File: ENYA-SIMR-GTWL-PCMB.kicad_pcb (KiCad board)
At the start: 4 copper layers, 116.2 x 60 mm, 127 parts, among them J1 USB_A_RA, J10 PICO_BLADE_1x6_MALE_RA_SMD, J11 PICO_BLADE_1x6_MALE_RA_SMD, J12 PICO_BLADE_1x14_MALE_RA_SMD, J13 PICO_BLADE_1x14_MALE_RA_SMD, J14 USB_WIRE_POINT, J2 TC2050-FP_PROG, J3 PICO_BLADE_1x3_MALE_RA_SMD, J4 PICO_BLADE_1x3_MALE_RA_SMD, J5 PICO_BLADE_1x3_MALE_RA_SMD, J6 PICO_BLADE_1x3_MALE_RA_SMD, J7 PICO_BLADE_1x3_MALE_RA_SMD, J8 PICO_BLADE_1x5_MALE_RA_SMD, J9 PICO_BLADE_1x5_MALE_RA_SMD, Q9 2N7002, SW1 56DP30-01-1-AJN, SW2 56DP30-01-1-AJN, SW3 56DP30-01-1-AJN, SW4 56DP30-01-1-AJN, U1 USB2512B, U4 AP22653W6-7_ILIM_2.1A_SOT-23-6, U5 STM32F303RET6TR, U6 LM393BIDR, U7 MCP1725_3.3V_500mA_DFN-8, U8 TPD2EUSB30_5.5V_8V_SOT-3, U9 TPD2EUSB30_5.5V_8V_SOT-3, Y1 ABM10_24MHz_10pF_SMD4_2.5x2.0, Y2 ABM10_32MHz_10pF_SMD4_2.5x2.0

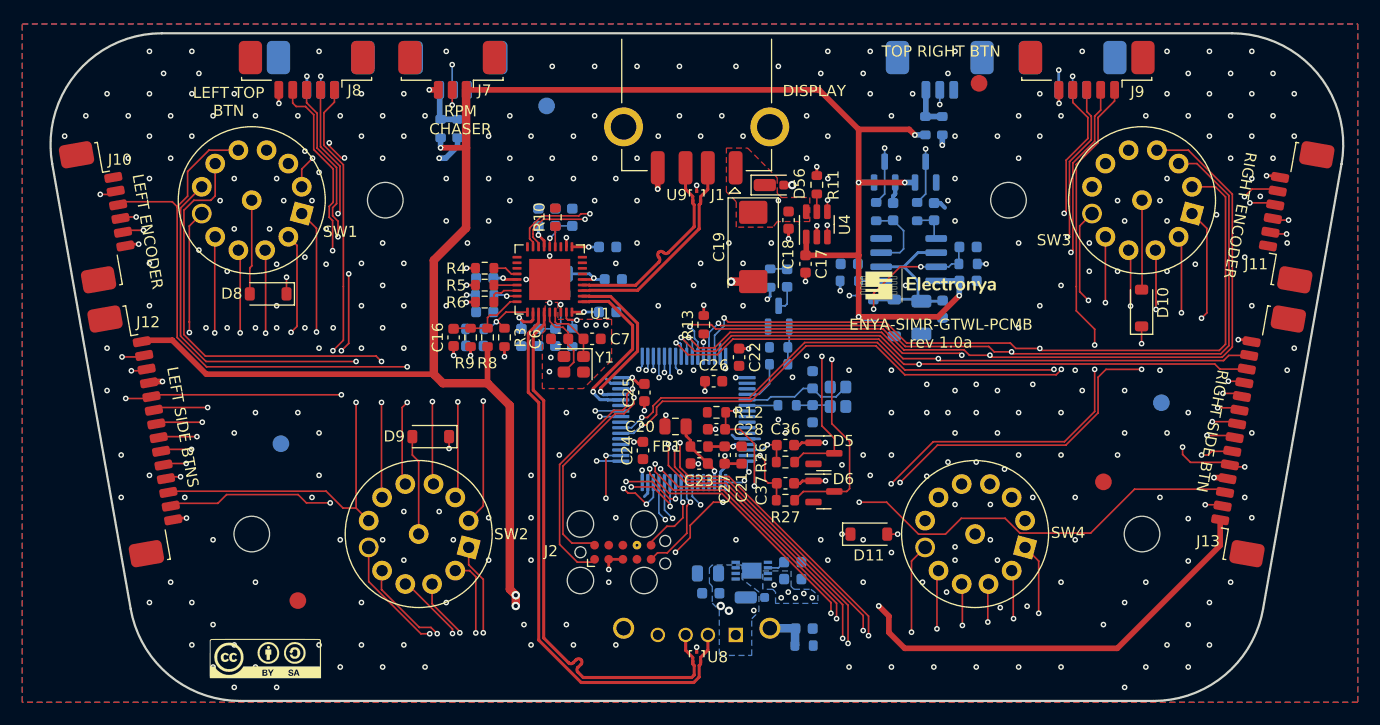
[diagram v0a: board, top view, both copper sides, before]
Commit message: rework for encoder instead of selector switch
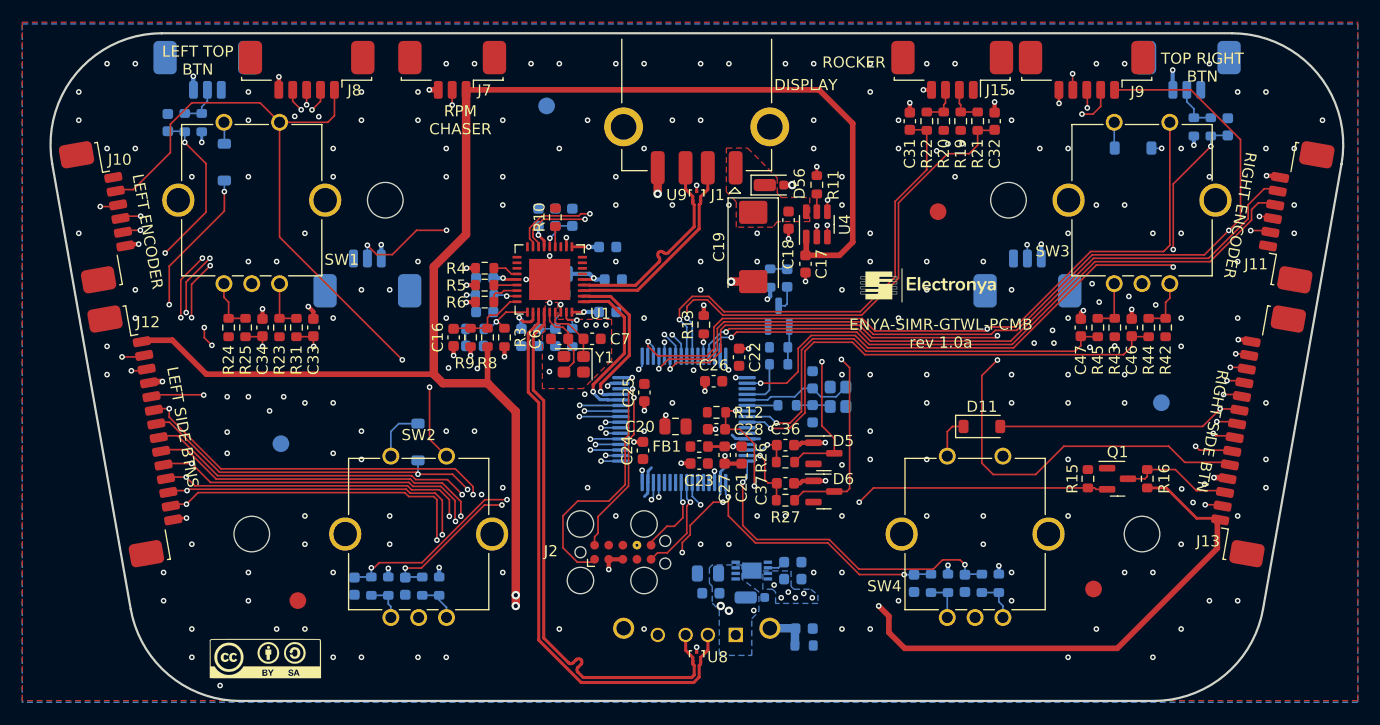
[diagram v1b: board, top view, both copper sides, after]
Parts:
- removed D3, D4: BAV99_SOT-23, Package_TO_SOT_SMD:SOT-23
- removed U6: LM393BIDR, Package_SO:SOIC-8_3.9x4.9mm_P1.27mm
- removed Z1: MMSZ5222BT1G, Diode_SMD:D_SOD-123
- added C45: 10nF_CER_0603_50V, Capacitor_SMD:C_0603_1608Metric, B.Cu at (177.8, 154.4)
- added C46: 10nF_CER_0603_50V, Capacitor_SMD:C_0603_1608Metric, F.Cu at (247.6, 131.2)
- added C47: 10nF_CER_0603_50V, Capacitor_SMD:C_0603_1608Metric, F.Cu at (243.1, 131.2)
- added C48: 10nF_CER_0603_50V, Capacitor_SMD:C_0603_1608Metric, B.Cu at (232.6, 154.2)
- added C49: 10nF_CER_0603_50V, Capacitor_SMD:C_0603_1608Metric, B.Cu at (228.1, 154.2)
- added J15: PICO_BLADE_1x4_MALE_RA_SMD, ENYA_Connector_PicoBlade:PICO_BLADE_53261_1x4_SMD_RA_1.25MM, F.Cu at (231.5, 106.9)
- added Q1: BSS138, Package_TO_SOT_SMD:SOT-23, F.Cu at (246.4, 144.8)
- added R19: 10K_0603_100MW, Resistor_SMD:R_0603_1608Metric, F.Cu at (232.3, 112.6)
- added R20: 10K_0603_100MW, Resistor_SMD:R_0603_1608Metric, F.Cu at (230.7, 112.6)
- added R21: 0R_0603_100MW, Resistor_SMD:R_0603_1608Metric, F.Cu at (233.8, 112.6)
- added R22: 0R_0603_100MW, Resistor_SMD:R_0603_1608Metric, F.Cu at (229.2, 112.6)
- added R23: 10K_0603_100MW, Resistor_SMD:R_0603_1608Metric, F.Cu at (171.0, 131.2)
- added R31: 10K_0603_100MW, Resistor_SMD:R_0603_1608Metric, F.Cu at (172.6, 131.2)
- added R32: 10K_0603_100MW, Resistor_SMD:R_0603_1608Metric, B.Cu at (185.4, 154.4)
- added R33: 10K_0603_100MW, Resistor_SMD:R_0603_1608Metric, B.Cu at (180.8, 154.4)
- added R34: 10K_0603_100MW, Resistor_SMD:R_0603_1608Metric, B.Cu at (183.9, 154.4)
- added R35: 10K_0603_100MW, Resistor_SMD:R_0603_1608Metric, B.Cu at (179.3, 154.4)
- added R36: 10K_0603_100MW, Resistor_SMD:R_0603_1608Metric, B.Cu at (235.7, 154.2)
- added R37: 10K_0603_100MW, Resistor_SMD:R_0603_1608Metric, B.Cu at (231.1, 154.2)
- added R38: 10K_0603_100MW, Resistor_SMD:R_0603_1608Metric, B.Cu at (234.2, 154.2)
- added R42: 10K_0603_100MW, Resistor_SMD:R_0603_1608Metric, F.Cu at (250.7, 131.2)
- added R43: 10K_0603_100MW, Resistor_SMD:R_0603_1608Metric, F.Cu at (246.1, 131.2)
- added R44: 10K_0603_100MW, Resistor_SMD:R_0603_1608Metric, F.Cu at (249.1, 131.2)
- added R45: 10K_0603_100MW, Resistor_SMD:R_0603_1608Metric, F.Cu at (244.6, 131.2)
- C31, C32, R24, R25: moved to F.Cu
- C33, C34: value 100nF_CER_0603_50V -> 10nF_CER_0603_50V; moved to F.Cu
- C35: value 10uF_CER_1206_25V -> 10nF_CER_0603_50V; footprint Capacitor_SMD:C_1206_3216Metric -> Capacitor_SMD:C_0603_1608Metric
- D10, D8, D9: moved to B.Cu
- R15, R16: value 0R_0603_100MW -> 10K_0603_100MW; moved to F.Cu
- R17, R18: value 0R_0603_100MW -> 10K_0603_100MW
- R39: value 124R_0603_100MW -> 10K_0603_100MW
- SW1, SW2, SW3, SW4: value 56DP30-01-1-AJN -> PEC11H-4015F-S0016; footprint ENYA_Switch_Selector:56DP30-01-1-AJN_1P_12T -> ENYA_Encoder:PEC11H_Switch_Vertical
- moved R16 69.5 mm to (249.0, 144.8)
- moved R15 66.1 mm to (243.7, 144.8), turned to -90 degrees
- moved C38 65.7 mm to (161.0, 112.8)
- moved R25 65.2 mm to (168.0, 131.2), turned to 90 degrees
- moved R17 65.0 mm to (164.1, 112.8)
- moved C34 63.8 mm to (169.5, 131.2), turned to 90 degrees
- moved R28 62.6 mm to (162.5, 112.8)
- moved R24 55.9 mm to (166.5, 131.2), turned to -90 degrees
- moved C35 52.3 mm to (182.3, 154.4)
- moved C33 48.5 mm to (174.1, 131.2), turned to 90 degrees
- moved C39 27.5 mm to (256.3, 113.2)
- moved R29 27.5 mm to (254.7, 113.2)
- moved R39 25.2 mm to (229.6, 154.2), turned to -90 degrees
- moved R18 22.6 mm to (253.2, 113.2)
- moved J6 22.2 mm to (252.6, 106.9)
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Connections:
- C31 pad 1: +2.5V -> /MCU/ROCKER_RIGHT
- C32 pad 1: +5V -> /MCU/ROCKER_LEFT
- C33 pad 1: /MCU/SHIFTER_DOWN -> /BUTTONS_ENCODERS_LEDS/TC_ENC_B
- C34 pad 1: /MCU/SHIFTER_UP -> /BUTTONS_ENCODERS_LEDS/TC_ENC_A
- C35 pad 1: +2.5V -> /BUTTONS_ENCODERS_LEDS/TC1_ENC_B
- C38 pad 1: Net-(U6A-+) -> /MCU/SHIFTER_DOWN
- C39 pad 1: Net-(U6B-+) -> /MCU/SHIFTER_UP
- D10 pad 1: /BUTTONS_ENCODERS_LEDS/BTN_COL2 -> Net-(D10-K)
- D10 pad 2: Net-(D10-A) -> /BUTTONS_ENCODERS_LEDS/BTN_ROW2
- D11 pad 1: /BUTTONS_ENCODERS_LEDS/BTN_COL3 -> Net-(D11-K)
- D11 pad 2: Net-(D11-A) -> /BUTTONS_ENCODERS_LEDS/BTN_ROW3
- D8 pad 1: /BUTTONS_ENCODERS_LEDS/BTN_COL0 -> Net-(D8-K)
- D8 pad 2: Net-(D8-A) -> /BUTTONS_ENCODERS_LEDS/BTN_ROW0
- D9 pad 1: /BUTTONS_ENCODERS_LEDS/BTN_COL1 -> Net-(D9-K)
- D9 pad 2: Net-(D9-A) -> /BUTTONS_ENCODERS_LEDS/BTN_ROW1
- J1 pad SH: Earth -> GND
- J10 pad 2: /BUTTONS_ENCODERS_LEDS/BTN_COL5 -> /BUTTONS_ENCODERS_LEDS/BTN_COL0
- J10 pad 3: /BUTTONS_ENCODERS_LEDS/BTN_ROW8 -> /BUTTONS_ENCODERS_LEDS/BTN_ROW7
- J11 pad 2: /BUTTONS_ENCODERS_LEDS/BTN_COL6 -> /BUTTONS_ENCODERS_LEDS/BTN_COL1
- J11 pad 3: /BUTTONS_ENCODERS_LEDS/BTN_ROW8 -> /BUTTONS_ENCODERS_LEDS/BTN_ROW3
- J12 pad 5: /BUTTONS_ENCODERS_LEDS/BTN_COL5 -> /BUTTONS_ENCODERS_LEDS/BTN_COL2
- J13 pad 5: /BUTTONS_ENCODERS_LEDS/BTN_COL6 -> /BUTTONS_ENCODERS_LEDS/BTN_COL3
- J5 pad 1: Net-(J5-Pin_1) -> +3.3V
- J6 pad 1: Net-(J6-Pin_1) -> +3.3V
- J8 pad 1: /BUTTONS_ENCODERS_LEDS/BTN_COL4 -> /BUTTONS_ENCODERS_LEDS/BTN_COL0
- J8 pad 2: /BUTTONS_ENCODERS_LEDS/BTN_ROW0 -> /BUTTONS_ENCODERS_LEDS/BTN_ROW4
- J8 pad 3: /BUTTONS_ENCODERS_LEDS/BTN_ROW1 -> /BUTTONS_ENCODERS_LEDS/BTN_ROW5
- J8 pad 4: /BUTTONS_ENCODERS_LEDS/BTN_ROW2 -> /BUTTONS_ENCODERS_LEDS/BTN_ROW6
- J9 pad 1: /BUTTONS_ENCODERS_LEDS/BTN_COL4 -> /BUTTONS_ENCODERS_LEDS/BTN_COL1
- J9 pad 2: /BUTTONS_ENCODERS_LEDS/BTN_ROW3 -> /BUTTONS_ENCODERS_LEDS/BTN_ROW0
- J9 pad 3: /BUTTONS_ENCODERS_LEDS/BTN_ROW4 -> /BUTTONS_ENCODERS_LEDS/BTN_ROW1
- J9 pad 4: /BUTTONS_ENCODERS_LEDS/BTN_ROW5 -> /BUTTONS_ENCODERS_LEDS/BTN_ROW2
- R15 pad 1: +5V -> +3.3V
- R15 pad 2: Net-(J5-Pin_1) -> Net-(Q1-S)
- R16 pad 1: +3.3V -> +5V
- R16 pad 2: Net-(J5-Pin_1) -> /BUTTONS_ENCODERS_LEDS/LED_D0
- R17 pad 1: +5V -> +3.3V
- R17 pad 2: Net-(J6-Pin_1) -> Net-(J5-Pin_2)
- R18 pad 2: Net-(J6-Pin_1) -> Net-(J6-Pin_2)
- R24 pad 1: +3.3V -> Net-(R24-Pad1)
- R24 pad 2: /MCU/SHIFTER_DOWN -> +3.3V
- R25 pad 1: +3.3V -> /BUTTONS_ENCODERS_LEDS/TC_ENC_A
- R25 pad 2: /MCU/SHIFTER_UP -> Net-(R24-Pad1)
- R28 pad 1: Net-(U6A-+) -> /MCU/SHIFTER_DOWN
- R29 pad 1: Net-(U6B-+) -> /MCU/SHIFTER_UP
- R39 pad 1: +5V -> /BUTTONS_ENCODERS_LEDS/MAP_ENC_A
- R39 pad 2: +2.5V -> Net-(R37-Pad1)
- U5 pad 16: /MCU/SHIFTER_DOWN -> /BUTTONS_ENCODERS_LEDS/MAP_ENC_B
- U5 pad 17: /MCU/SHIFTER_UP -> /BUTTONS_ENCODERS_LEDS/MAP_ENC_A
- U5 pad 2: unconnected-(U5-PC13-Pad2) -> /MCU/SHIFTER_UP
- U5 pad 21: /MCU/LED_CLK -> unconnected-(U5-PA5-Pad21)
- U5 pad 23: /BUTTONS_ENCODERS_LEDS/LED_D0 -> Net-(Q1-S)
- U5 pad 26: /BUTTONS_ENCODERS_LEDS/BTN_COL0 -> unconnected-(U5-PB0-Pad26)
- U5 pad 27: /BUTTONS_ENCODERS_LEDS/BTN_COL1 -> unconnected-(U5-PB1-Pad27)
- U5 pad 28: /BUTTONS_ENCODERS_LEDS/BTN_COL2 -> unconnected-(U5-PB2-Pad28)
- U5 pad 29: /BUTTONS_ENCODERS_LEDS/BTN_COL3 -> /BUTTONS_ENCODERS_LEDS/TC1_ENC_B
- U5 pad 30: /BUTTONS_ENCODERS_LEDS/BTN_COL4 -> /BUTTONS_ENCODERS_LEDS/TC1_ENC_A
- U5 pad 33: /BUTTONS_ENCODERS_LEDS/BTN_COL5 -> /BUTTONS_ENCODERS_LEDS/BTN_ROW0
- U5 pad 34: /BUTTONS_ENCODERS_LEDS/BTN_COL6 -> /BUTTONS_ENCODERS_LEDS/BTN_ROW1
- U5 pad 35: unconnected-(U5-PB14-Pad35) -> /BUTTONS_ENCODERS_LEDS/BTN_ROW2
- U5 pad 36: unconnected-(U5-PB15-Pad36) -> /BUTTONS_ENCODERS_LEDS/BTN_ROW3
- U5 pad 37: unconnected-(U5-PC6-Pad37) -> /BUTTONS_ENCODERS_LEDS/BTN_ROW4
- U5 pad 38: /BUTTONS_ENCODERS_LEDS/RIGHT_ENC_A -> /BUTTONS_ENCODERS_LEDS/BTN_ROW5
- U5 pad 39: /BUTTONS_ENCODERS_LEDS/RIGHT_ENC_B -> /BUTTONS_ENCODERS_LEDS/BTN_ROW6
- U5 pad 40: unconnected-(U5-PC9-Pad40) -> /BUTTONS_ENCODERS_LEDS/BTN_ROW7
- U5 pad 41: /BUTTONS_ENCODERS_LEDS/LEFT_ENC_A -> /BUTTONS_ENCODERS_LEDS/TC_ENC_A
- U5 pad 42: /BUTTONS_ENCODERS_LEDS/LEFT_ENC_B -> /BUTTONS_ENCODERS_LEDS/TC_ENC_B
- U5 pad 43: unconnected-(U5-PA10-Pad43) -> /MCU/SHIFTER_DOWN
- U5 pad 50: /BUTTONS_ENCODERS_LEDS/BTN_ROW0 -> unconnected-(U5-PA15-Pad50)
- U5 pad 51: /BUTTONS_ENCODERS_LEDS/BTN_ROW1 -> /BUTTONS_ENCODERS_LEDS/BTN_COL0
- U5 pad 52: /BUTTONS_ENCODERS_LEDS/BTN_ROW2 -> /BUTTONS_ENCODERS_LEDS/BTN_COL1
- U5 pad 53: /BUTTONS_ENCODERS_LEDS/BTN_ROW3 -> /BUTTONS_ENCODERS_LEDS/BTN_COL2
- U5 pad 54: /BUTTONS_ENCODERS_LEDS/BTN_ROW4 -> /BUTTONS_ENCODERS_LEDS/BTN_COL3
- U5 pad 55: /BUTTONS_ENCODERS_LEDS/BTN_ROW5 -> /BUTTONS_ENCODERS_LEDS/LEFT_ENC_B
- U5 pad 56: /BUTTONS_ENCODERS_LEDS/BTN_ROW6 -> /BUTTONS_ENCODERS_LEDS/LEFT_ENC_A
- U5 pad 57: /BUTTONS_ENCODERS_LEDS/BTN_ROW7 -> /MCU/ROCKER_RIGHT
- U5 pad 58: /BUTTONS_ENCODERS_LEDS/BTN_ROW8 -> /MCU/ROCKER_LEFT
- U5 pad 59: /BUTTONS_ENCODERS_LEDS/BTN_ROW9 -> unconnected-(U5-PB7-Pad59)
- U5 pad 61: /BUTTONS_ENCODERS_LEDS/BTN_ROW10 -> /BUTTONS_ENCODERS_LEDS/RIGHT_ENC_B
- U5 pad 62: /BUTTONS_ENCODERS_LEDS/BTN_ROW11 -> /BUTTONS_ENCODERS_LEDS/RIGHT_ENC_A
- U5 pad 8: unconnected-(U5-PC0-Pad8) -> /BUTTONS_ENCODERS_LEDS/ABS_ENC_A
- U5 pad 9: unconnected-(U5-PC1-Pad9) -> /BUTTONS_ENCODERS_LEDS/ABS_ENC_B
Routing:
- net /BUTTONS_ENCODERS_LEDS/BTN_ROW8: track 174.6 -> 0.00 mm, vias 5 -> 0
- net /BUTTONS_ENCODERS_LEDS/BTN_ROW11: track 158.9 -> 0.00 mm, vias 4 -> 0
- net /BUTTONS_ENCODERS_LEDS/BTN_ROW9: track 158.5 -> 0.00 mm, vias 5 -> 0
- net /BUTTONS_ENCODERS_LEDS/BTN_ROW10: track 155.3 -> 0.00 mm, vias 3 -> 0
- net /BUTTONS_ENCODERS_LEDS/BTN_COL4: track 139.3 -> 0.00 mm, vias 6 -> 0
- net /BUTTONS_ENCODERS_LEDS/BTN_COL0: track 54.9 -> 163.7 mm, vias 5 -> 4
- net /BUTTONS_ENCODERS_LEDS/BTN_COL6: track 104.2 -> 0.00 mm, vias 5 -> 0
- net /BUTTONS_ENCODERS_LEDS/BTN_COL5: track 68.6 -> 0.00 mm, vias 4 -> 0
- net /BUTTONS_ENCODERS_LEDS/BTN_ROW5: track 248.4 -> 187.1 mm, vias 10 -> 7
- net /BUTTONS_ENCODERS_LEDS/BTN_COL1: track 26.7 -> 85.1 mm
- net /BUTTONS_ENCODERS_LEDS/BTN_ROW1: track 235.6 -> 177.7 mm, vias 10 -> 5
- net /BUTTONS_ENCODERS_LEDS/BTN_ROW2: track 236.0 -> 181.3 mm, vias 10 -> 5
- net /BUTTONS_ENCODERS_LEDS/BTN_ROW4: track 238.4 -> 185.0 mm, vias 10 -> 7
- net /BUTTONS_ENCODERS_LEDS/BTN_ROW3: track 236.1 -> 185.7 mm, vias 10 -> 4
- net /BUTTONS_ENCODERS_LEDS/BTN_COL3: track 20.7 -> 70.4 mm, vias 2 -> 3
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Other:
- board text added: "ROCKER"
- board text added: "SHIFTER UP"
- board text removed: "SHIFT UP"
